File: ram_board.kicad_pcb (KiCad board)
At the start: 4 copper layers, 72.6 x 31.6 mm, 26 parts, among them J1 Bus, J2 PWR, SW1 Config, U1 IS61LV5128AL-10TLI, U2 SST39VF040-70-4C-NHE, U3 74LVC2G240, U4 74LVC2G240, U5 74LVC2G32

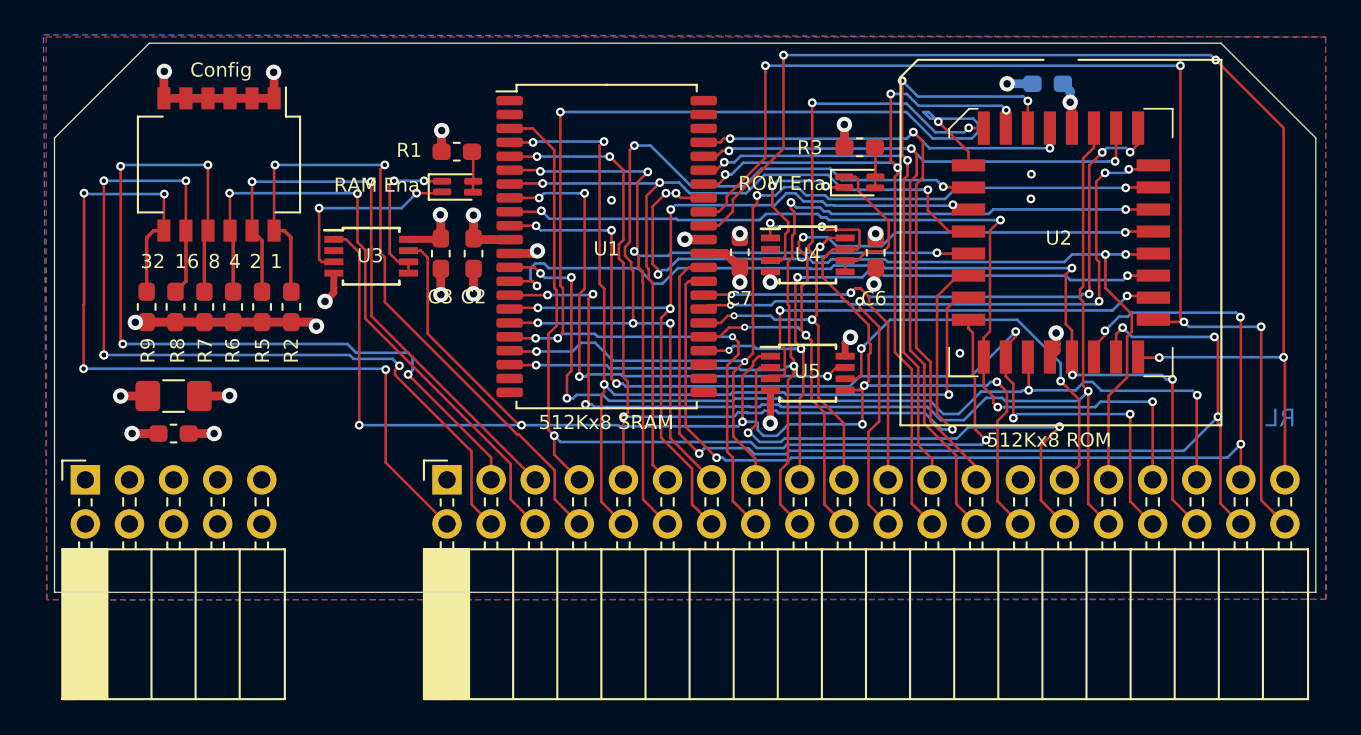
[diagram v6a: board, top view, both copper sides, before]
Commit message: fixed up LED's and muxed signals
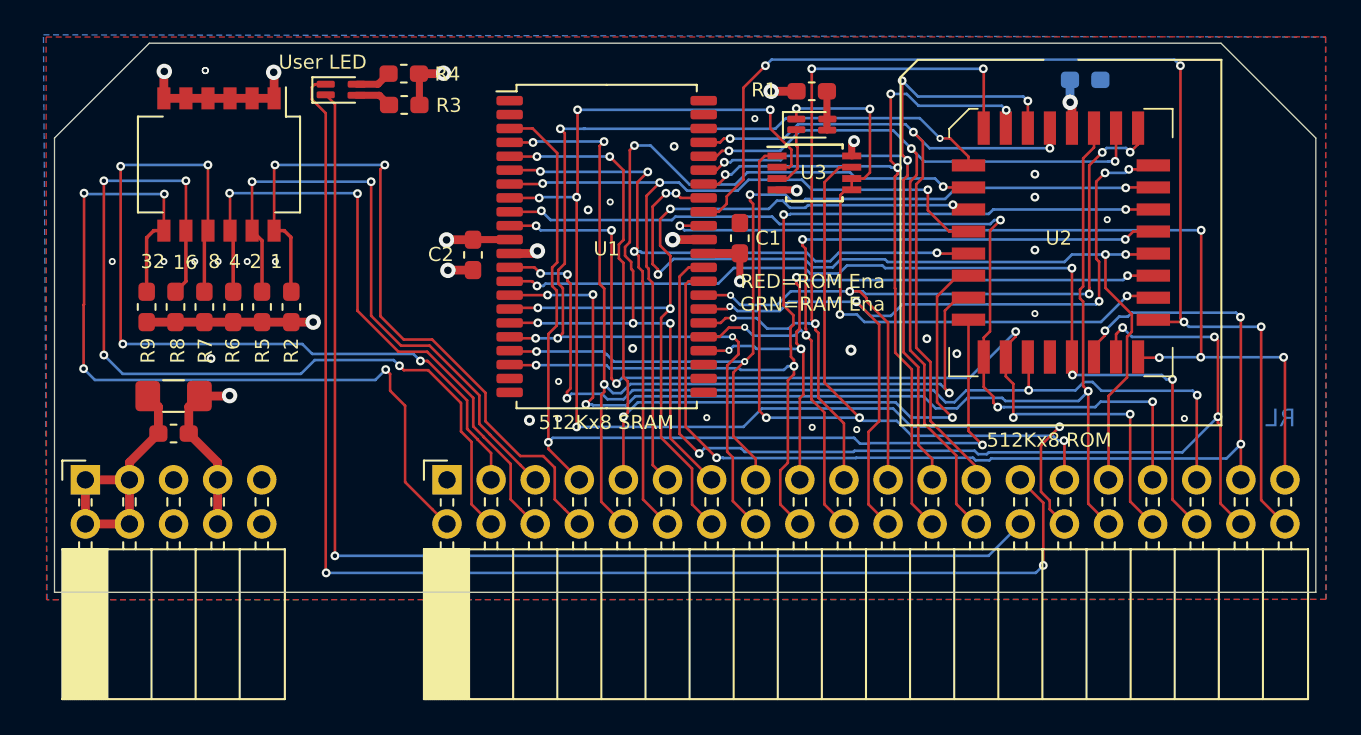
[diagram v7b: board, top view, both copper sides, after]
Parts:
- removed C6, C7: 100nF, Capacitor_SMD:C_0603_1608Metric_Pad1.05x0.95mm_HandSolder
- removed D3: LED, LED_SMD:LED_2C_0603_1608Metric_Pad1.05x0.95mm_HandSolder
- removed U4: 74LVC2G240, Package_SO:TSSOP-8_3x3mm_P0.65mm
- removed U5: 74LVC2G32, Package_SO:TSSOP-8_3x3mm_P0.65mm
- added D1: LED, LED_SMD:LED_2C_0603_1608Metric_Pad1.05x0.95mm_HandSolder, F.Cu at (134.0, 75.2)
- added R4: 360R, Resistor_SMD:R_0603_1608Metric_Pad1.05x0.95mm_HandSolder, F.Cu at (137.6, 74.3)
- C1: moved to F.Cu
- C3: moved to B.Cu
- moved C3 38.4 mm to (176.8, 74.6), turned to 0 degrees
- moved R3 26.3 mm to (137.6, 76.1), turned to 0 degrees
- moved U3 26.0 mm to (161.2, 80.0)
- moved R1 20.7 mm to (161.1, 75.3)
- moved D2 20.7 mm to (161.1, 77.2)
- moved C1 19.8 mm to (156.9, 83.7), turned to 90 degrees
- moved C2 0.08 mm to (141.6, 84.7)
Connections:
- D2 pad 2: Net-(D2-Pad2) -> /~ROM
- J1 pad 27: (no net) -> /LED_R
- J1 pad 28: /~ENA -> /LED_G
- J1 pad 29: /~ROM -> /~ENA
- U1 pad 8: Net-(U1-Pad8) -> /~RAM
- U2 pad 22: Net-(U2-Pad22) -> /~ROM
- U3 pad 2: (no net) -> /~RAM
- U3 pad 5: Net-(D2-Pad2) -> /~ROM
- U3 pad 6: Net-(D2-Pad2) -> /~ROM
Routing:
- net /LED_R: track 0.00 -> 76.1 mm, vias 0 -> 2
- net /LED_G: track 0.00 -> 67.0 mm, vias 0 -> 1
- net /~ENA: track 98.3 -> 52.4 mm, vias 8 -> 3
- net /~RAM: track 29.9 -> 73.1 mm, vias 2 -> 6
- net Net-(U1-Pad8): track 30.7 -> 0.00 mm, vias 4 -> 0
- net Net-(U2-Pad22): track 26.7 -> 0.00 mm, vias 2 -> 0
- net /D6: track 71.5 -> 54.3 mm, vias 4 -> 5
- net /~ROM: track 23.3 -> 36.9 mm, vias 2 -> 4
- net Net-(D3-Pad4): track 9.87 -> 0.00 mm, vias 2 -> 0
- net Net-(D2-Pad2): track 9.00 -> 0.00 mm, vias 2 -> 0
- net Net-(D3-Pad2): track 8.93 -> 0.00 mm
- net /A7: track 71.2 -> 62.6 mm
- net Net-(D2-Pad4): track 11.3 -> 3.68 mm, vias 2 -> 0
- net GND: track 26.8 -> 31.4 mm, vias 19 -> 35
- net /A12: track 40.1 -> 44.7 mm
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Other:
- board text added: "RED=ROM Ena GRN=RAM Ena"
- board text added: "User LED"
- board text removed: "Config"
- board text removed: "RAM Ena"
- board text removed: "ROM Ena"

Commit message: added z80
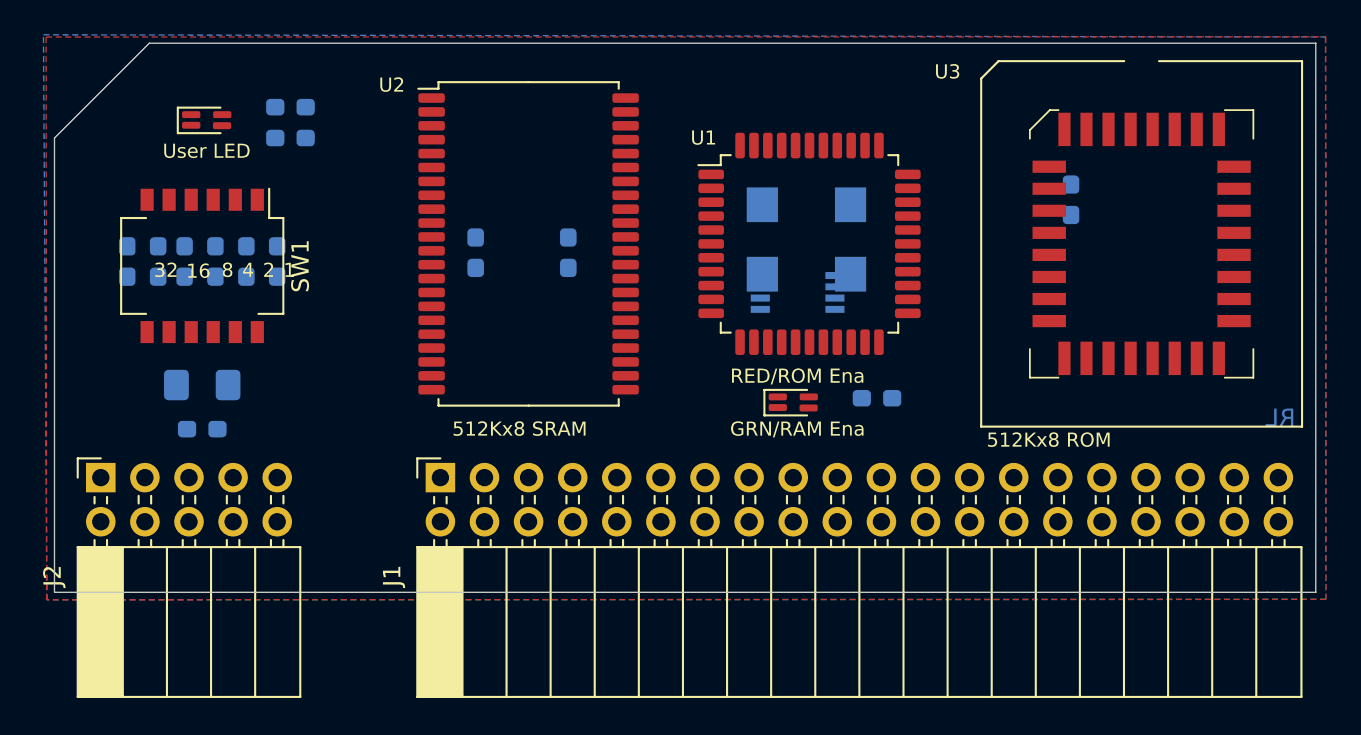
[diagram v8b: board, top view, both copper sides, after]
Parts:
- added U4: 74LVC2G240, Package_SO:TSSOP-8_3x3mm_P0.65mm, B.Cu at (160.3, 86.9)
- added X1: ASV-xxxMHz, Oscillator:Oscillator_SMD_Abracon_ASV-4Pin_7.0x5.1mm, B.Cu at (160.8, 83.8)
- C1: value 100nF -> 100uF; footprint Capacitor_SMD:C_0603_1608Metric_Pad1.05x0.95mm_HandSolder -> Capacitor_SMD:C_1206_3216Metric_Pad1.42x1.75mm_HandSolder; moved to B.Cu
- C2, C5, R1, R3, R5, R6, R7, R8, R9: moved to B.Cu
- C4: value 100uF -> 100nF; footprint Capacitor_SMD:C_1206_3216Metric_Pad1.42x1.75mm_HandSolder -> Capacitor_SMD:C_0603_1608Metric_Pad1.05x0.95mm_HandSolder; moved to B.Cu
- R2: value 10K -> 360R; moved to B.Cu
- R4: value 360R -> 10K; moved to B.Cu
- U1: value IS61LV5128AL-10TLI -> CPU - Z84C0010AEG; footprint Package_SO:TSOP-II-44_10.16x18.41mm_P0.8mm -> Package_QFP:LQFP-44_10x10mm_P0.8mm
- U2: value SST39VF040-70-4C-NHE -> IS61LV5128AL-10TLI; footprint Package_LCC:PLCC-32_SMD-Socket -> Package_SO:TSOP-II-44_10.16x18.41mm_P0.8mm
- U3: value 74LVC2G240 -> SST39VF040-70-4C-NHE; footprint Package_SO:TSSOP-8_3x3mm_P0.65mm -> Package_LCC:PLCC-32_SMD-Socket
- moved C4 52.9 mm to (176.0, 81.5), turned to 90 degrees
- moved C3 36.5 mm to (141.7, 84.6), turned to 90 degrees
- moved C1 32.1 mm to (126.0, 92.2), turned to 0 degrees
- moved R3 32.0 mm to (164.8, 93.0)
- moved U2 30.7 mm to (144.8, 84.1)
- moved R1 30.0 mm to (131.1, 76.2), turned to 0 degrees
- moved C5 25.0 mm to (147.1, 84.6), turned to 270 degrees
- moved U3 19.3 mm to (180.1, 84.1)
- moved C2 18.5 mm to (126.0, 94.7), turned to 0 degrees
- moved D2 16.0 mm to (160.0, 93.2)
- moved R4 13.0 mm to (130.3, 85.1), turned to 90 degrees
- moved U1 11.7 mm to (161.0, 84.1)
- moved R2 9.73 mm to (131.1, 78.0), turned to 0 degrees
- moved D1 7.94 mm to (126.2, 77.0)
- moved SW1 5.92 mm to (126.0, 85.3)
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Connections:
- R1 pad 1: Net-(D2-Pad1) -> Net-(D1-Pad1)
- R2 pad 1: /SW1_0 -> Net-(D1-Pad3)
- R3 pad 1: Net-(D1-Pad3) -> Net-(D2-Pad1)
- R4 pad 1: Net-(D1-Pad1) -> /SW1_0
- U1 pad 11: +3V3 -> (no net)
- U1 pad 12: GND -> (no net)
- U1 pad 13: /D2 -> (no net)
- U1 pad 14: /D3 -> (no net)
- U1 pad 15: /~WR -> (no net)
- U1 pad 16: /A5 -> (no net)
- U1 pad 17: /A6 -> (no net)
- U1 pad 18: /A7 -> /~RD
- U1 pad 19: /A8 -> /~WR
- U1 pad 2: (no net) -> /D4
- U1 pad 20: /A9 -> (no net)
- U1 pad 26: /A10 -> GND
- U1 pad 27: /A11 -> /A0
- U1 pad 28: /A12 -> /A1
- U1 pad 29: /A13 -> /A2
- U1 pad 3: /A0 -> /D3
- U1 pad 30: /A14 -> /A3
- U1 pad 31: /D4 -> /A4
- U1 pad 32: /D5 -> /A5
- U1 pad 33: +3V3 -> (no net)
- U1 pad 34: GND -> /A6
- U1 pad 35: /D6 -> /A7
- U1 pad 36: /D7 -> /A8
- U1 pad 37: /~RD -> /A9
- U1 pad 38: /A15 -> /A10
- U1 pad 39: /A16 -> (no net)
- U1 pad 4: /A1 -> /D5
- U1 pad 40: /A17 -> /A11
- U1 pad 41: /A18 -> /A12
- U1 pad 42: (no net) -> /A13
- U1 pad 43: (no net) -> /A14
- U1 pad 44: (no net) -> /A15
- U1 pad 5: /A2 -> /D6
- U1 pad 6: /A3 -> (no net)
- U1 pad 7: /A4 -> /D2
- U1 pad 8: /~RAM -> /D7
- U2 pad 1: /A18 -> (no net)
- U2 pad 10: /A2 -> /D1
- U2 pad 11: /A1 -> +3V3
- U2 pad 12: /A0 -> GND
- U2 pad 13: /D0 -> /D2
- U2 pad 14: /D1 -> /D3
- U2 pad 15: /D2 -> /~WR
- U2 pad 16: GND -> /A5
- U2 pad 17: /D3 -> /A6
- U2 pad 18: /D4 -> /A7
- U2 pad 19: /D5 -> /A8
- U2 pad 2: /A16 -> (no net)
- U2 pad 20: /D6 -> /A9
- U2 pad 21: /D7 -> (no net)
- U2 pad 22: /~ROM -> (no net)
- U2 pad 23: /A10 -> (no net)
- U2 pad 24: /~RD -> (no net)
- U2 pad 25: /A11 -> (no net)
- U2 pad 26: /A9 -> /A10
- U2 pad 27: /A8 -> /A11
- U2 pad 28: /A13 -> /A12
- U2 pad 29: /A14 -> /A13
- U2 pad 3: /A15 -> /A0
- U2 pad 30: /A17 -> /A14
- U2 pad 31: /~WR -> /D4
- U2 pad 32: +3V3 -> /D5
- U2 pad 4: /A12 -> /A1
- U2 pad 5: /A7 -> /A2
- U2 pad 6: /A6 -> /A3
- U2 pad 7: /A5 -> /A4
- U2 pad 8: /A4 -> /~RAM
- U2 pad 9: /A3 -> /D0
- U3 pad 1: /~ENA -> /A18
- U3 pad 2: /~RAM -> /A16
- U3 pad 3: Net-(D2-Pad4) -> /A15
- U3 pad 4: GND -> /A12
- U3 pad 5: /~ROM -> /A7
- U3 pad 6: /~ROM -> /A6
- U3 pad 7: /~ENA -> /A5
- U3 pad 8: +3V3 -> /A4
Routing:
- net /LED_R: track 76.1 -> 0.00 mm, vias 2 -> 0
- net /~RAM: track 73.1 -> 0.00 mm, vias 6 -> 0
- net /D7: track 67.8 -> 0.00 mm, vias 4 -> 0
- net /LED_G: track 67.0 -> 0.00 mm, vias 1 -> 0
- net /~WR: track 65.1 -> 0.00 mm, vias 4 -> 0
- net /A7: track 62.6 -> 0.00 mm, vias 5 -> 0
- net /D5: track 62.1 -> 0.00 mm, vias 4 -> 0
- net /D4: track 62.0 -> 0.00 mm, vias 4 -> 0
- net /D1: track 58.2 -> 0.00 mm, vias 6 -> 0
- net /A9: track 57.0 -> 0.00 mm, vias 4 -> 0
- net /A0: track 56.2 -> 0.00 mm, vias 2 -> 0
- net /D2: track 55.5 -> 0.00 mm, vias 5 -> 0
- net /A1: track 55.5 -> 0.00 mm, vias 4 -> 0
- net /A8: track 55.1 -> 0.00 mm, vias 4 -> 0
- net /A2: track 54.4 -> 0.00 mm, vias 4 -> 0
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- added copper zone on In1.Cu, net GND
- removed copper zone on 3V3, net +3V3
- removed copper zone on GND, net GND
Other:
- outline, holes or cut-outs redrawn
- board text added: "GRN/RAM Ena"
- board text added: "RED/ROM Ena"
- board text removed: "RED=ROM Ena GRN=RAM Ena"
